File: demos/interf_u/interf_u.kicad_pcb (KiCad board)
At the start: 2 copper layers, 25 parts, among them P1 DB25FEMELLE, U1 74LS245, U2 74LS688, U3 74LS541, U5 628128, U8 EP600, U9 4003APG120, X1 8MHz

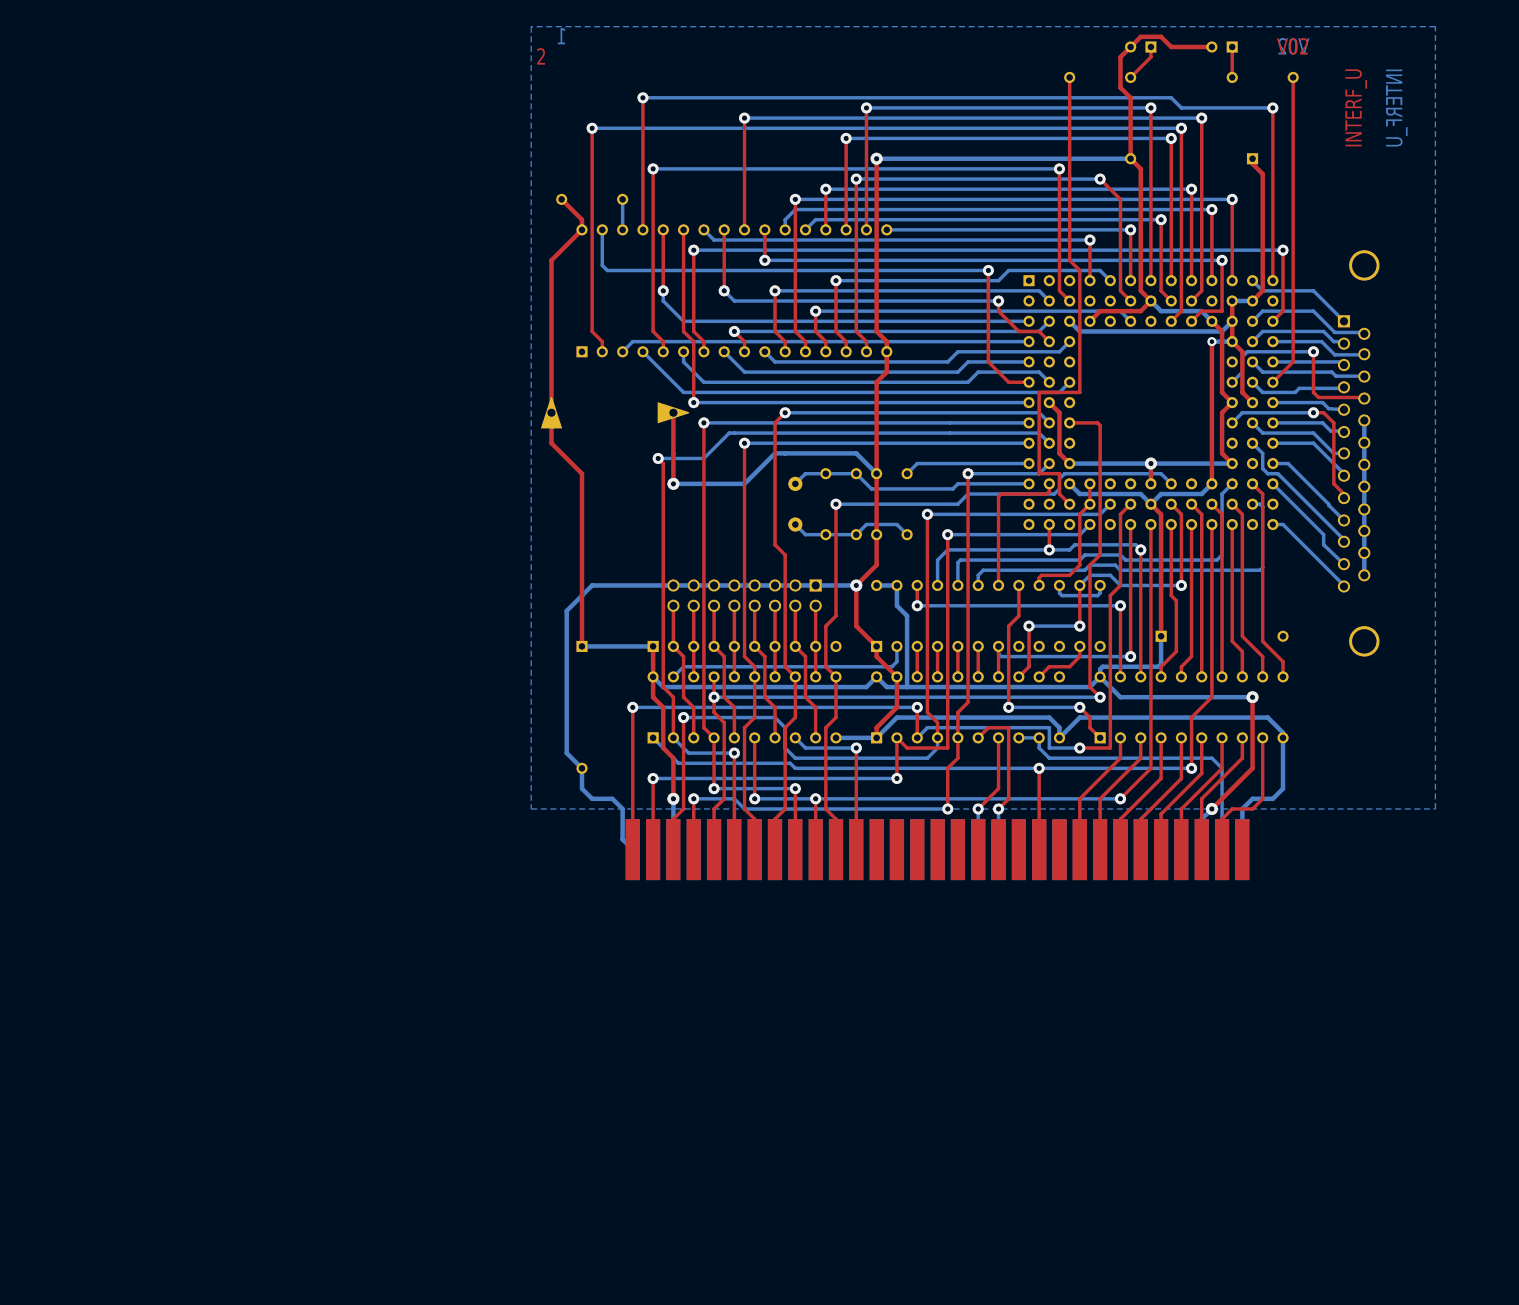
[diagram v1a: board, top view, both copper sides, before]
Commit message: Eeschema: fix Bug #1210120
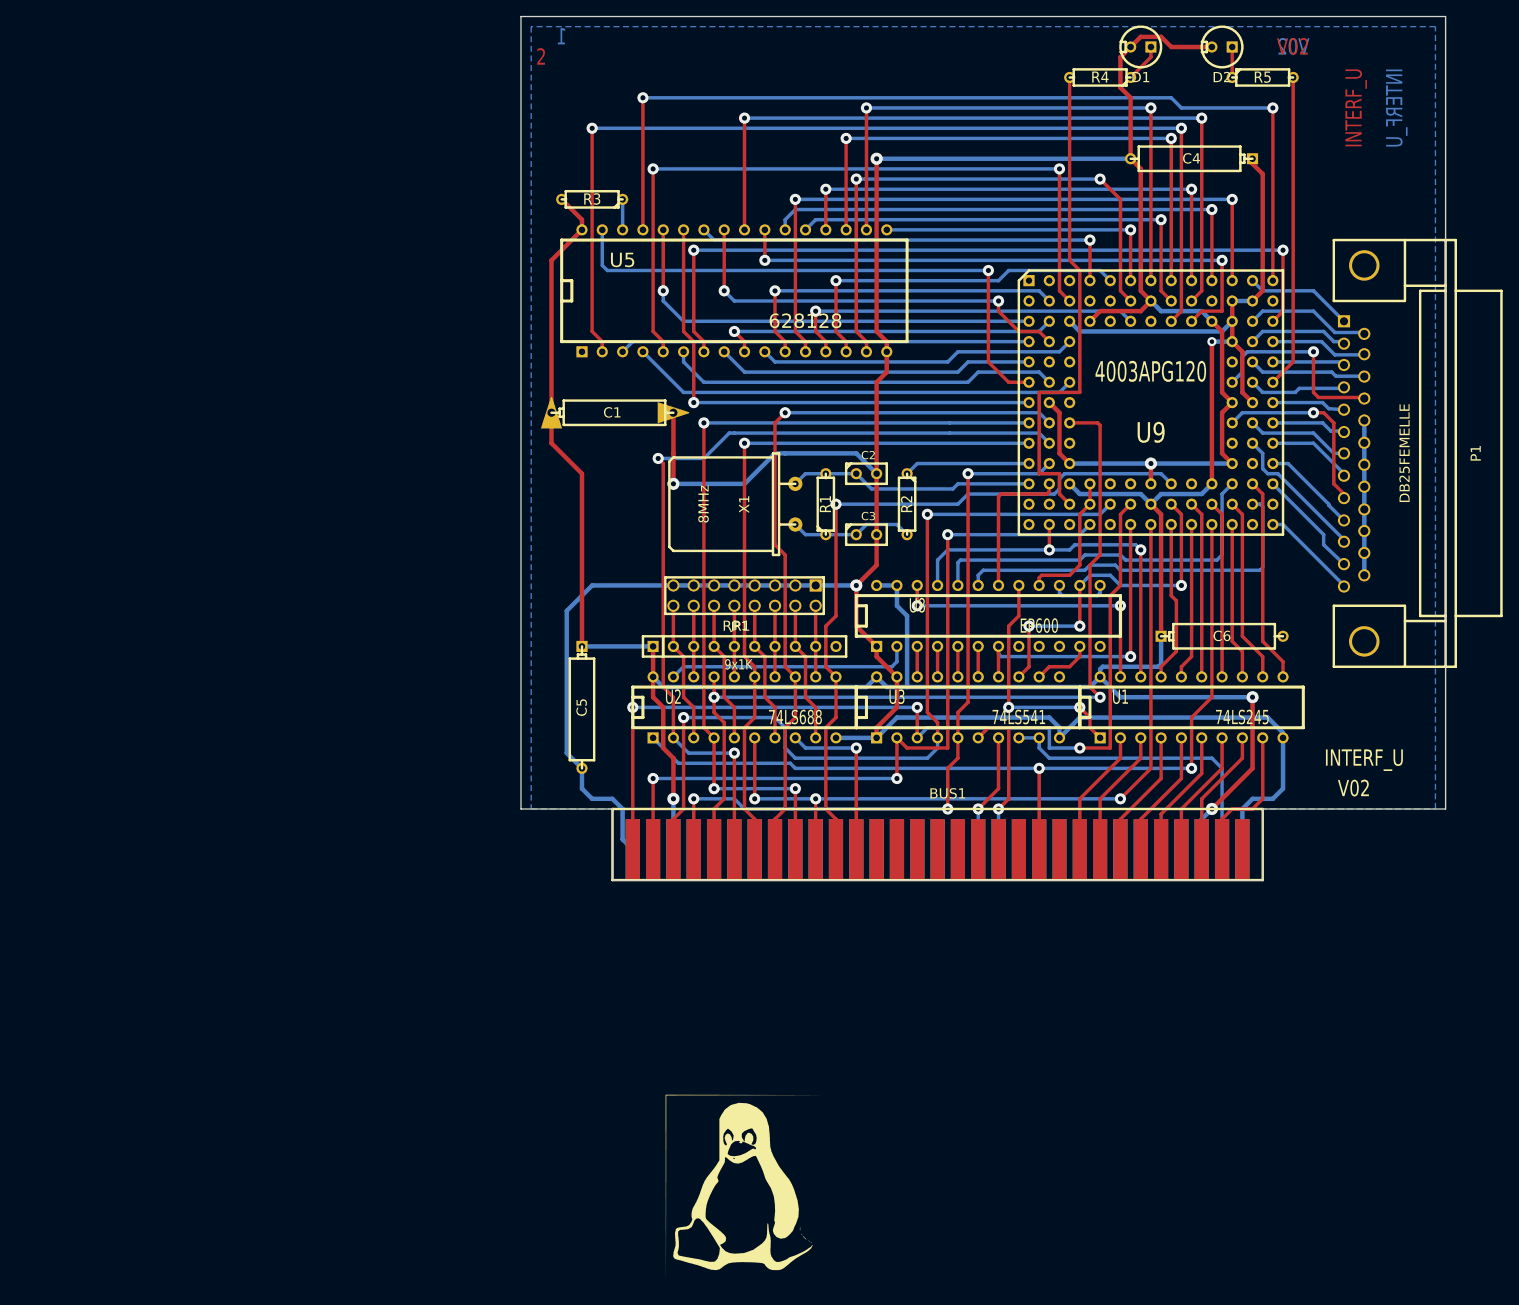
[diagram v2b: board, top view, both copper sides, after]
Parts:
- moved G1 55.4 mm to (107.1, 180.5)
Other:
- board outline added: 115.6 x 108 mm

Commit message: Pcbnew: Fix a bug when reading a netlist which forces pcbnew to read lib files to find a footprint even if the right footprint is already loaded (which explains the long time to load netlists) Netlist dialog: add option to report only most important messages. Useful for large boards. class REPORTER: add features to allow a basic message filtering (flags to report all/warning/error messages) Fix Bug #1214599 ( tools are deselected on Move command )
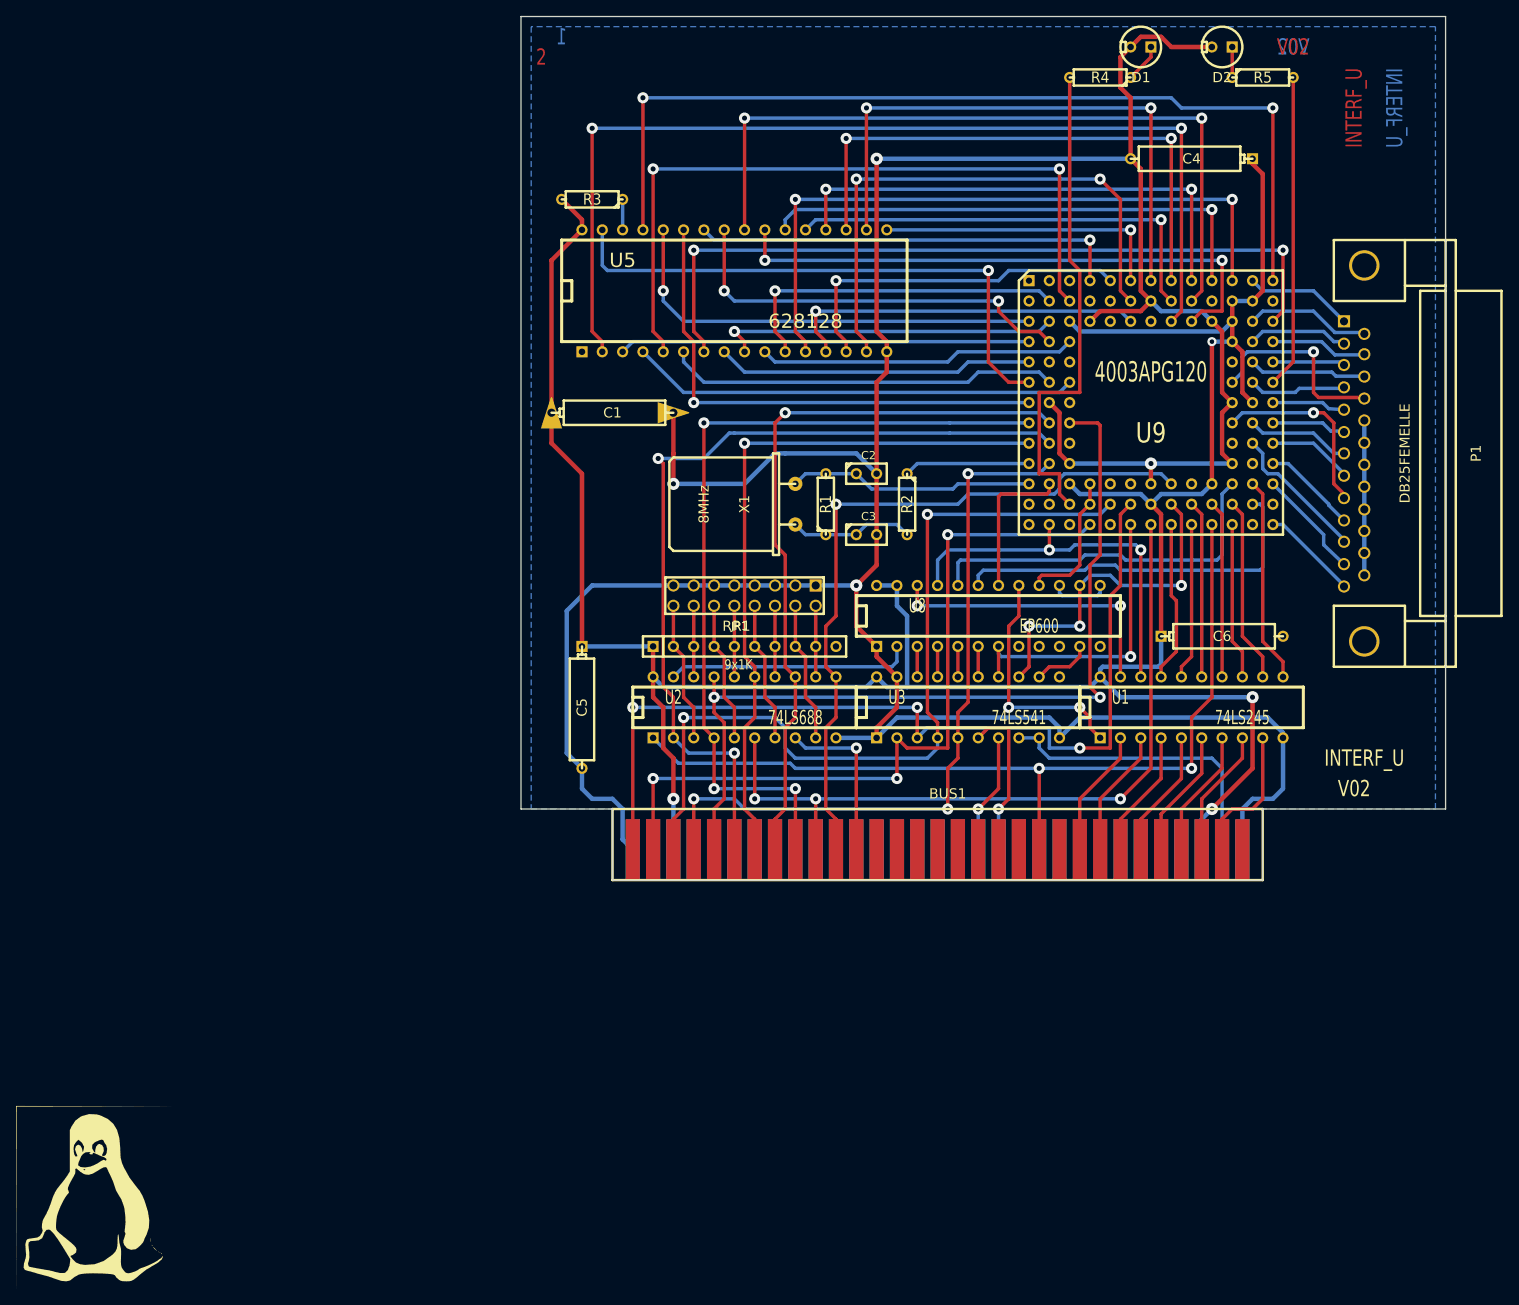
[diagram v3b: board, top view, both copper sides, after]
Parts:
- U1, U2, U3: footprint 20dip300 -> DIP-20__300
- U8: footprint 24dip300 -> DIP-24__300
- moved G1 81.2 mm to (25.9, 181.9)
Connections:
- BUS1 pad 10: (no net) -> N-0000026
- BUS1 pad 11: (no net) -> N-0000025
- BUS1 pad 12: (no net) -> N-0000018
- BUS1 pad 15: (no net) -> N-0000014
- BUS1 pad 16: (no net) -> N-0000013
- BUS1 pad 17: (no net) -> N-0000012
- BUS1 pad 18: (no net) -> N-0000011
- BUS1 pad 19: (no net) -> N-0000010
- BUS1 pad 20: (no net) -> N-000009
- BUS1 pad 21: (no net) -> N-000008
- BUS1 pad 22: (no net) -> N-000007
- BUS1 pad 23: (no net) -> N-000006
- BUS1 pad 24: (no net) -> N-000005
- BUS1 pad 25: (no net) -> N-000004
- BUS1 pad 26: (no net) -> N-000003
- BUS1 pad 27: (no net) -> N-000002
- BUS1 pad 28: (no net) -> N-000001
- BUS1 pad 30: (no net) -> N-0000042
- BUS1 pad 32: (no net) -> N-0000041
- BUS1 pad 4: (no net) -> N-0000032
- BUS1 pad 41: (no net) -> N-0000040
- BUS1 pad 43: (no net) -> N-0000024
- BUS1 pad 44: (no net) -> N-0000039
- BUS1 pad 45: (no net) -> N-0000038
- BUS1 pad 46: (no net) -> N-0000037
- BUS1 pad 47: (no net) -> N-0000036
- BUS1 pad 48: (no net) -> N-0000035
- BUS1 pad 49: (no net) -> N-0000034
- BUS1 pad 5: (no net) -> N-0000031
- BUS1 pad 50: (no net) -> N-0000033
- BUS1 pad 6: (no net) -> N-0000030
- BUS1 pad 7: (no net) -> N-0000029
- BUS1 pad 8: (no net) -> N-0000028
- BUS1 pad 9: (no net) -> N-0000027
- RR1 pad 10: (no net) -> N-00000155
- U3 pad 11: (no net) -> N-0000062
- U8 pad 10: (no net) -> N-0000058
- U8 pad 8: (no net) -> N-0000060
- U8 pad 9: (no net) -> N-0000059
- U9 pad A1: (no net) -> N-0000048
- U9 pad A2: (no net) -> N-0000047
- U9 pad A3: (no net) -> N-0000044
- U9 pad B1: (no net) -> N-0000049
- U9 pad B10: (no net) -> N-00000143
- U9 pad B13: (no net) -> N-00000104
- U9 pad B4: (no net) -> N-0000045
- U9 pad B5: (no net) -> N-0000043
- U9 pad C5: (no net) -> N-0000046
- U9 pad E11: (no net) -> N-00000135
- U9 pad E2: (no net) -> N-0000051
- U9 pad E3: (no net) -> N-0000050
- U9 pad J11: (no net) -> N-00000136
- U9 pad J3: (no net) -> N-00000126
- U9 pad K12: (no net) -> N-00000138
- U9 pad L5: (no net) -> N-00000129
- U9 pad L6: (no net) -> N-00000141
- U9 pad L9: (no net) -> N-00000142
- U9 pad M1: (no net) -> N-00000132
- U9 pad M2: (no net) -> N-00000124
- U9 pad N1: (no net) -> N-00000133
- U9 pad N12: (no net) -> N-00000140
- U9 pad N3: (no net) -> N-00000127
- U9 pad N5: (no net) -> N-00000130

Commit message: Minor fixes: specctra export: skip malformed circles (having a radius = 0)  in board outline creation, which can crash 3d-viewer or vrml export. dialog_fp_lib_table: remember during a session the last open table (global or local). drawing_tool: fix compil warning Update demos.
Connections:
- BUS1 pad 10: N-0000026 -> (no net)
- BUS1 pad 11: N-0000025 -> (no net)
- BUS1 pad 12: N-0000018 -> (no net)
- BUS1 pad 15: N-0000014 -> (no net)
- BUS1 pad 16: N-0000013 -> (no net)
- BUS1 pad 17: N-0000012 -> (no net)
- BUS1 pad 18: N-0000011 -> (no net)
- BUS1 pad 19: N-0000010 -> (no net)
- BUS1 pad 20: N-000009 -> (no net)
- BUS1 pad 21: N-000008 -> (no net)
- BUS1 pad 22: N-000007 -> (no net)
- BUS1 pad 23: N-000006 -> (no net)
- BUS1 pad 24: N-000005 -> (no net)
- BUS1 pad 25: N-000004 -> (no net)
- BUS1 pad 26: N-000003 -> (no net)
- BUS1 pad 27: N-000002 -> (no net)
- BUS1 pad 28: N-000001 -> (no net)
- BUS1 pad 30: N-0000042 -> (no net)
- BUS1 pad 32: N-0000041 -> (no net)
- BUS1 pad 4: N-0000032 -> (no net)
- BUS1 pad 41: N-0000040 -> (no net)
- BUS1 pad 43: N-0000024 -> (no net)
- BUS1 pad 44: N-0000039 -> (no net)
- BUS1 pad 45: N-0000038 -> (no net)
- BUS1 pad 46: N-0000037 -> (no net)
- BUS1 pad 47: N-0000036 -> (no net)
- BUS1 pad 48: N-0000035 -> (no net)
- BUS1 pad 49: N-0000034 -> (no net)
- BUS1 pad 5: N-0000031 -> (no net)
- BUS1 pad 50: N-0000033 -> (no net)
- BUS1 pad 6: N-0000030 -> (no net)
- BUS1 pad 7: N-0000029 -> (no net)
- BUS1 pad 8: N-0000028 -> (no net)
- BUS1 pad 9: N-0000027 -> (no net)
- RR1 pad 10: N-00000155 -> (no net)
- U3 pad 11: N-0000062 -> (no net)
- U8 pad 10: N-0000058 -> (no net)
- U8 pad 8: N-0000060 -> (no net)
- U8 pad 9: N-0000059 -> (no net)
- U9 pad A1: N-0000048 -> (no net)
- U9 pad A2: N-0000047 -> (no net)
- U9 pad A3: N-0000044 -> (no net)
- U9 pad B1: N-0000049 -> (no net)
- U9 pad B10: N-00000143 -> (no net)
- U9 pad B13: N-00000104 -> (no net)
- U9 pad B4: N-0000045 -> (no net)
- U9 pad B5: N-0000043 -> (no net)
- U9 pad C5: N-0000046 -> (no net)
- U9 pad E11: N-00000135 -> (no net)
- U9 pad E2: N-0000051 -> (no net)
- U9 pad E3: N-0000050 -> (no net)
- U9 pad J11: N-00000136 -> (no net)
- U9 pad J3: N-00000126 -> (no net)
- U9 pad K12: N-00000138 -> (no net)
- U9 pad L5: N-00000129 -> (no net)
- U9 pad L6: N-00000141 -> (no net)
- U9 pad L9: N-00000142 -> (no net)
- U9 pad M1: N-00000132 -> (no net)
- U9 pad M2: N-00000124 -> (no net)
- U9 pad N1: N-00000133 -> (no net)
- U9 pad N12: N-00000140 -> (no net)
- U9 pad N3: N-00000127 -> (no net)
- U9 pad N5: N-00000130 -> (no net)

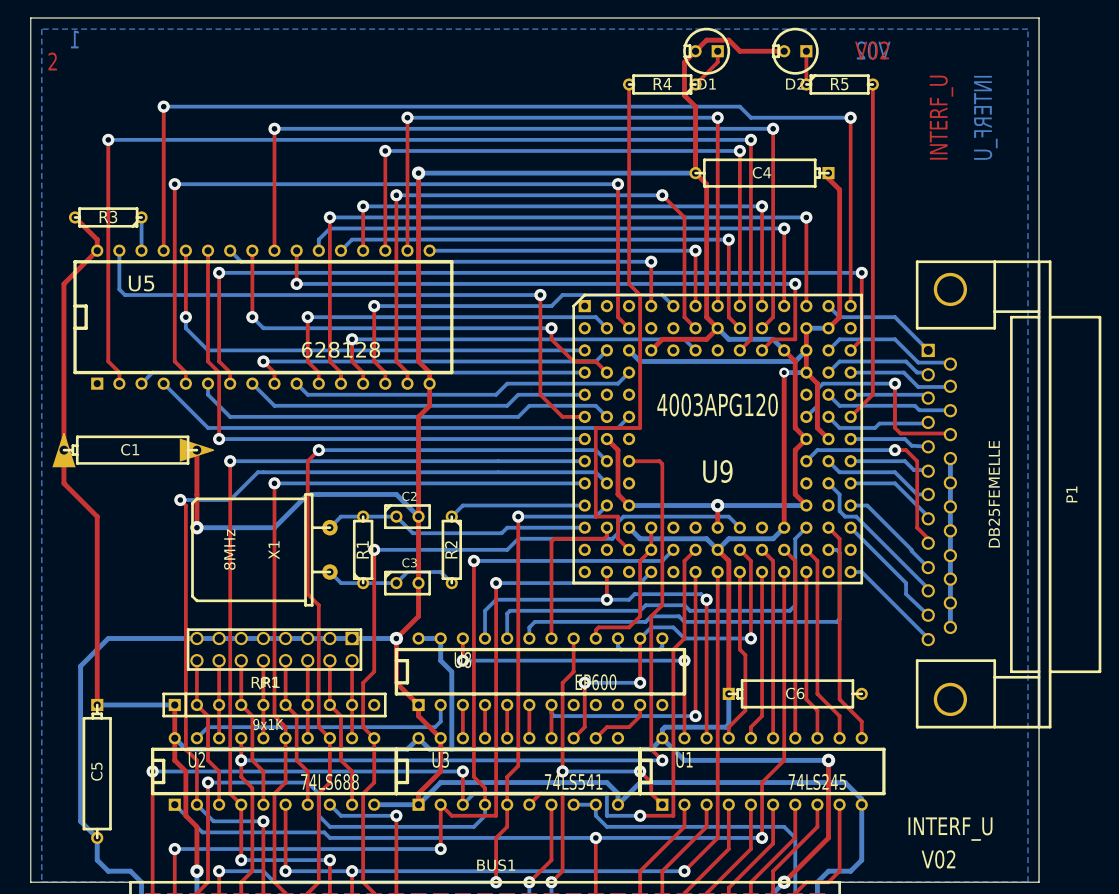
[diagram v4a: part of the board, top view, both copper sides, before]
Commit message: Demos: fix 3D models due to library changes. (fixes lp:1500956)
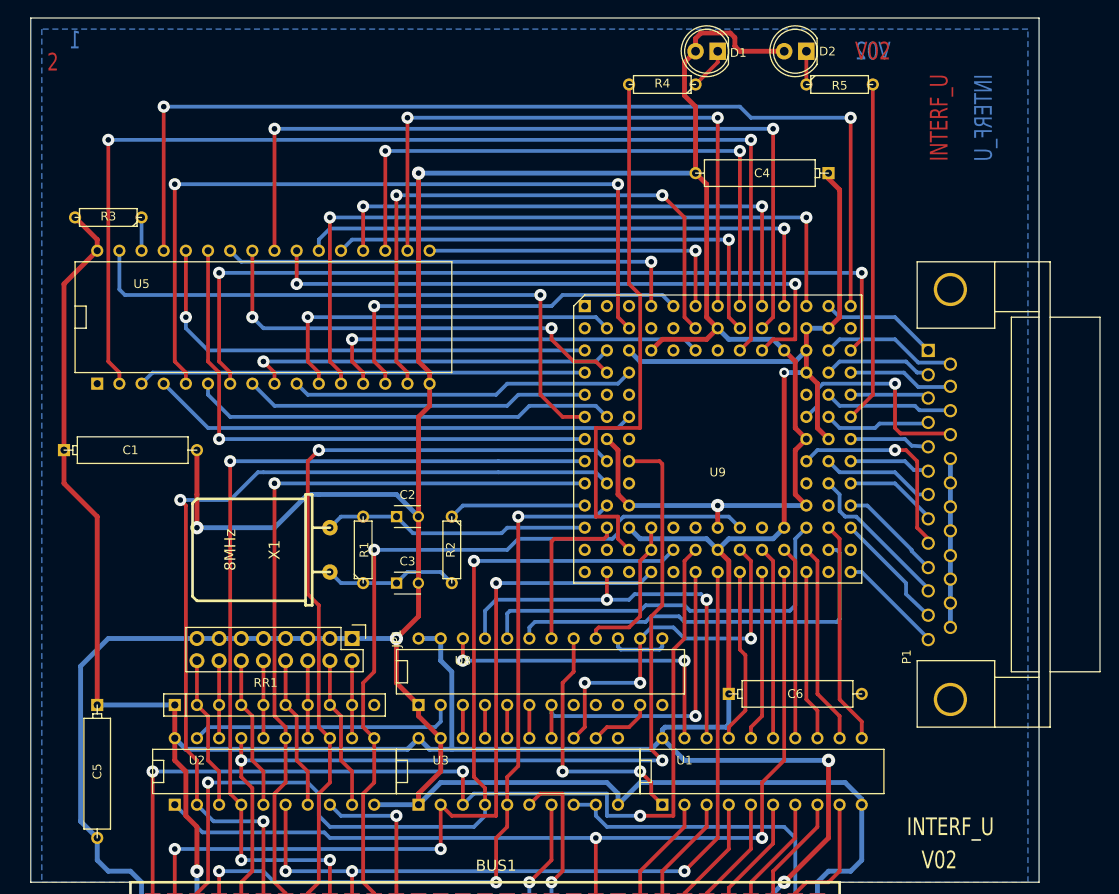
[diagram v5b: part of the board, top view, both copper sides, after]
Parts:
- C1, C4, C5, C6: footprint CP6 -> Discret:CP6
- C2, C3: footprint C1 -> Capacitors_ThroughHole:C_Disc_D3_P2.5
- D1, D2: footprint LEDV -> LEDs:LED-5MM
- JP1: footprint pin_array_8x2 -> Pin_Headers:Pin_Header_Straight_2x08
- P1: footprint DB25FC -> Connect:DB25FC
- R1, R2, R3, R4, R5: footprint R3 -> Discret:R3
- RR1: footprint r_pack9 -> Discret:r_pack9
- U1, U2, U3: footprint DIP-20__300 -> Sockets_DIP:DIP-20__300
- U5: footprint DIP-32__600 -> Sockets_DIP:DIP-32__600
- U8: footprint DIP-24__300 -> Sockets_DIP:DIP-24__300
- U9: footprint PGA120 -> Sockets:PGA120
- moved JP1 8.98 mm to (116.2, 105.4), turned to 270 degrees
- moved D1 1.27 mm to (158.1, 38.1)
- moved D2 1.27 mm to (168.3, 38.1)
- moved C2 1.25 mm to (121.3, 91.4)
- moved C3 1.25 mm to (121.3, 99.1)
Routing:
- net GND: track 430.5 -> 432.6 mm
